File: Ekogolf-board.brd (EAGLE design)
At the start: 87.3 x 64.8 mm, 11 parts

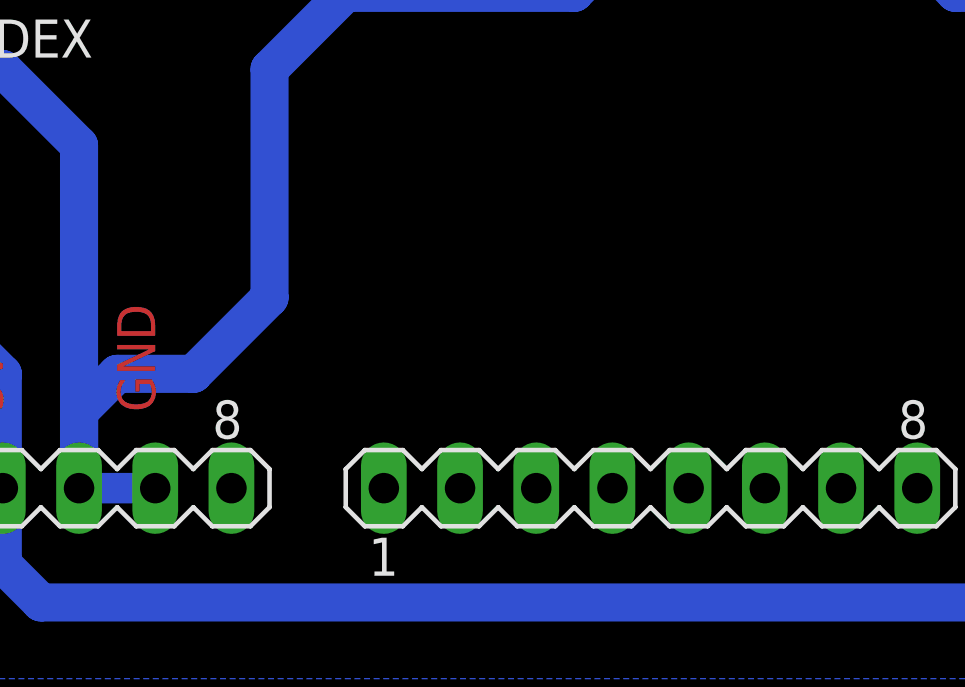
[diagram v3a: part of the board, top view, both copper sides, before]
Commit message: se agrega led indicador
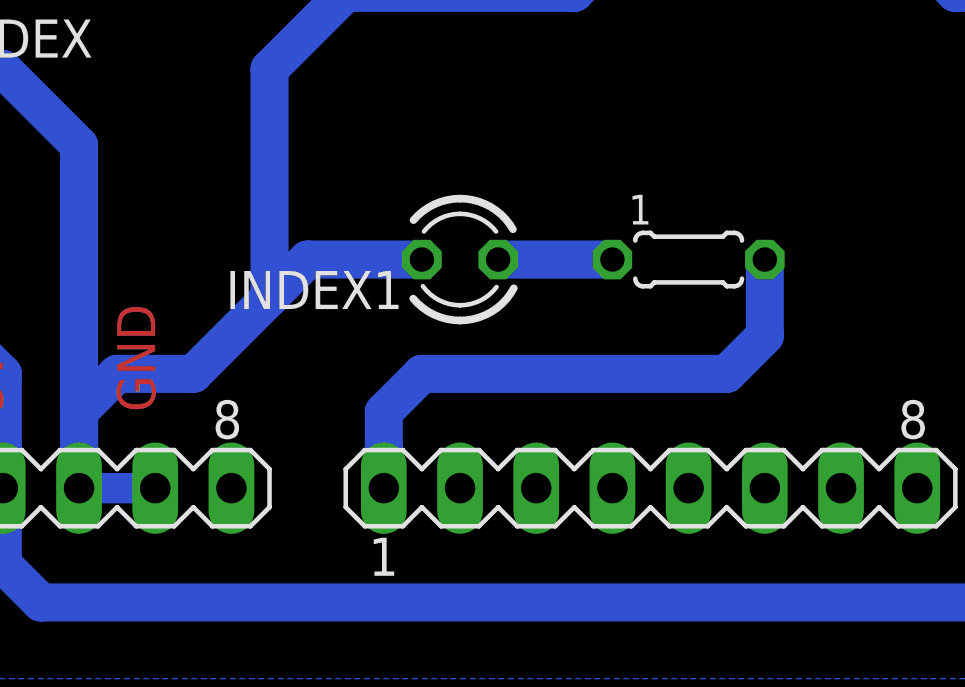
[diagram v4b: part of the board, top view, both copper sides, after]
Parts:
- added 1: (no value), rcl:0204/5
- added INDEX1: TLLY4400, led:LED3MM
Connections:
- new net N$2: 1.2, SV2.1
- new net N$3: 1.1, INDEX1.A
- net GND: now also INDEX1.K
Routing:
- net N$2: track 0.00 -> 18.8 mm
- net GND: track 121.3 -> 126.9 mm
- net N$3: track 0.00 -> 3.81 mm
- added copper zone on layer 16, net V
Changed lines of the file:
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@@
 <drawing>
 <settings>
-<setting alwaysvectorfont="yes"/>
+<setting alwaysvectorfont="no"/>
 <setting verticaltext="up"/>
 </settings>
@@
 <attribute name="VALUE" x="17.145" y="22.479" size="1.27" layer="27" ratio="10"/>
 </element>
+<element name="1" library="rcl" library_urn="urn:adsk.eagle:library:334" package="0204/5" package3d_urn="urn:adsk.eagle:package:23488/1" value="" x="41.91" y="17.78" smashed="yes">
+<attribute name="NAME" x="39.9034" y="18.9484" size="0.9906" layer="25" ratio="10"/>
+<attribute name="SPICEPREFIX" value="R" x="41.91" y="17.78" size="1.778" layer="27" display="off"/>
+<attribute name="VALUE" x="39.7764" y="15.4686" size="0.9906" layer="27" ratio="10"/>
+</element>
+<element name="INDEX1" library="led" library_urn="urn:adsk.eagle:library:259" package="LED3MM" package3d_urn="urn:adsk.eagle:package:15797/1" value="TLLY4400" x="34.29" y="17.78" smashed="yes" rot="R180">
+<attribute name="MF" value="VISHAY SEMICONDUCTOR" x="34.29" y="17.78" size="1.778" layer="27" rot="R180" display="off"/>
+<attribute name="NAME" x="32.385" y="17.399" size="1.27" layer="25" ratio="10" rot="R180"/>
+<attribute name="OC_FARNELL" value="1612439" x="34.29" y="17.78" size="1.778" layer="27" rot="R180" display="off"/>
+<attribute name="VALUE" x="32.385" y="19.431" size="1.27" layer="27" ratio="10" rot="R180"/>
+</element>
 </elements>
 <signals>
@@
 <wire x1="21.59" y1="21.59" x2="21.59" y2="10.16" width="1.27" layer="16"/>
 <wire x1="30.48" y1="36.83" x2="30.48" y2="26.67" width="1.27" layer="16"/>
-<polygon width="1.016" layer="16" isolate="0.8128">
-<vertex x="-6.35" y="64.77"/>
-<vertex x="-6.35" y="2.54"/>
-<vertex x="78.74" y="2.54"/>
-<vertex x="78.74" y="64.77"/>
-</polygon>
 <contactref element="SV1" pad="7"/>
 <wire x1="24.13" y1="10.16" x2="21.59" y2="10.16" width="1.016" layer="16"/>
+<contactref element="INDEX1" pad="K"/>
+<wire x1="29.21" y1="17.78" x2="27.94" y2="16.51" width="1.27" layer="16"/>
+<wire x1="33.02" y1="17.78" x2="29.21" y2="17.78" width="1.27" layer="16"/>
 </signal>
 <signal name="VCC">
@@
 <wire x1="8.89" y1="24.13" x2="13.97" y2="24.13" width="1.27" layer="16"/>
 </signal>
+<signal name="N$2">
+<contactref element="SV2" pad="1"/>
+<contactref element="1" pad="2"/>
+<wire x1="31.75" y1="12.7" x2="33.02" y2="13.97" width="1.27" layer="16"/>
+<wire x1="43.18" y1="13.97" x2="44.45" y2="15.24" width="1.27" layer="16"/>
+<wire x1="44.45" y1="15.24" x2="44.45" y2="17.78" width="1.27" layer="16"/>
+<wire x1="31.75" y1="10.16" x2="31.75" y2="12.7" width="1.27" layer="16"/>
+<wire x1="33.02" y1="13.97" x2="43.18" y2="13.97" width="1.27" layer="16"/>
+</signal>
+<signal name="N$3">
+<contactref element="INDEX1" pad="A"/>
+<contactref element="1" pad="1"/>
+<wire x1="35.56" y1="17.78" x2="39.37" y2="17.78" width="1.27" layer="16"/>
+</signal>
+<signal name="V">
+<polygon width="0.762" layer="16" isolate="1.27">
+<vertex x="-6.35" y="64.77"/>
+<vertex x="-6.35" y="2.54"/>
+<vertex x="78.74" y="2.54"/>
+<vertex x="78.74" y="64.77"/>
+</polygon>
+</signal>
 </signals>
